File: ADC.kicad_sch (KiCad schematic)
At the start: 28 parts, among them U107 ADR4540, U111 ADA4841-1

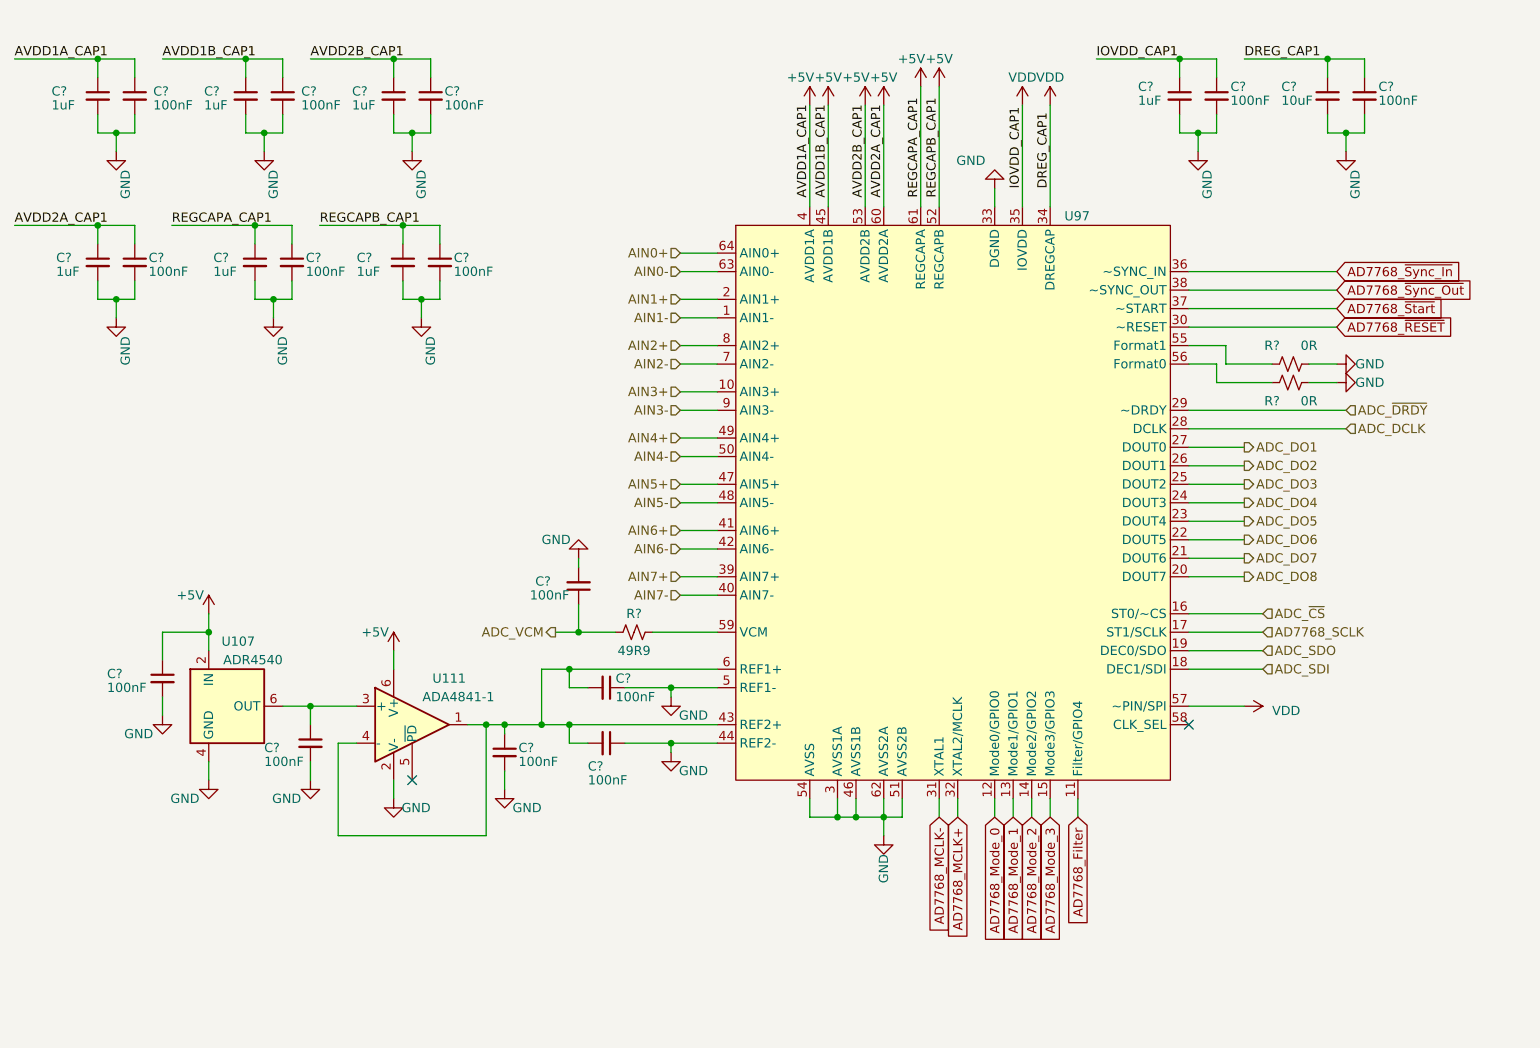
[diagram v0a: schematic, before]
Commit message: Updated Schematics with recent changes
Made Updates with recent suggestions.
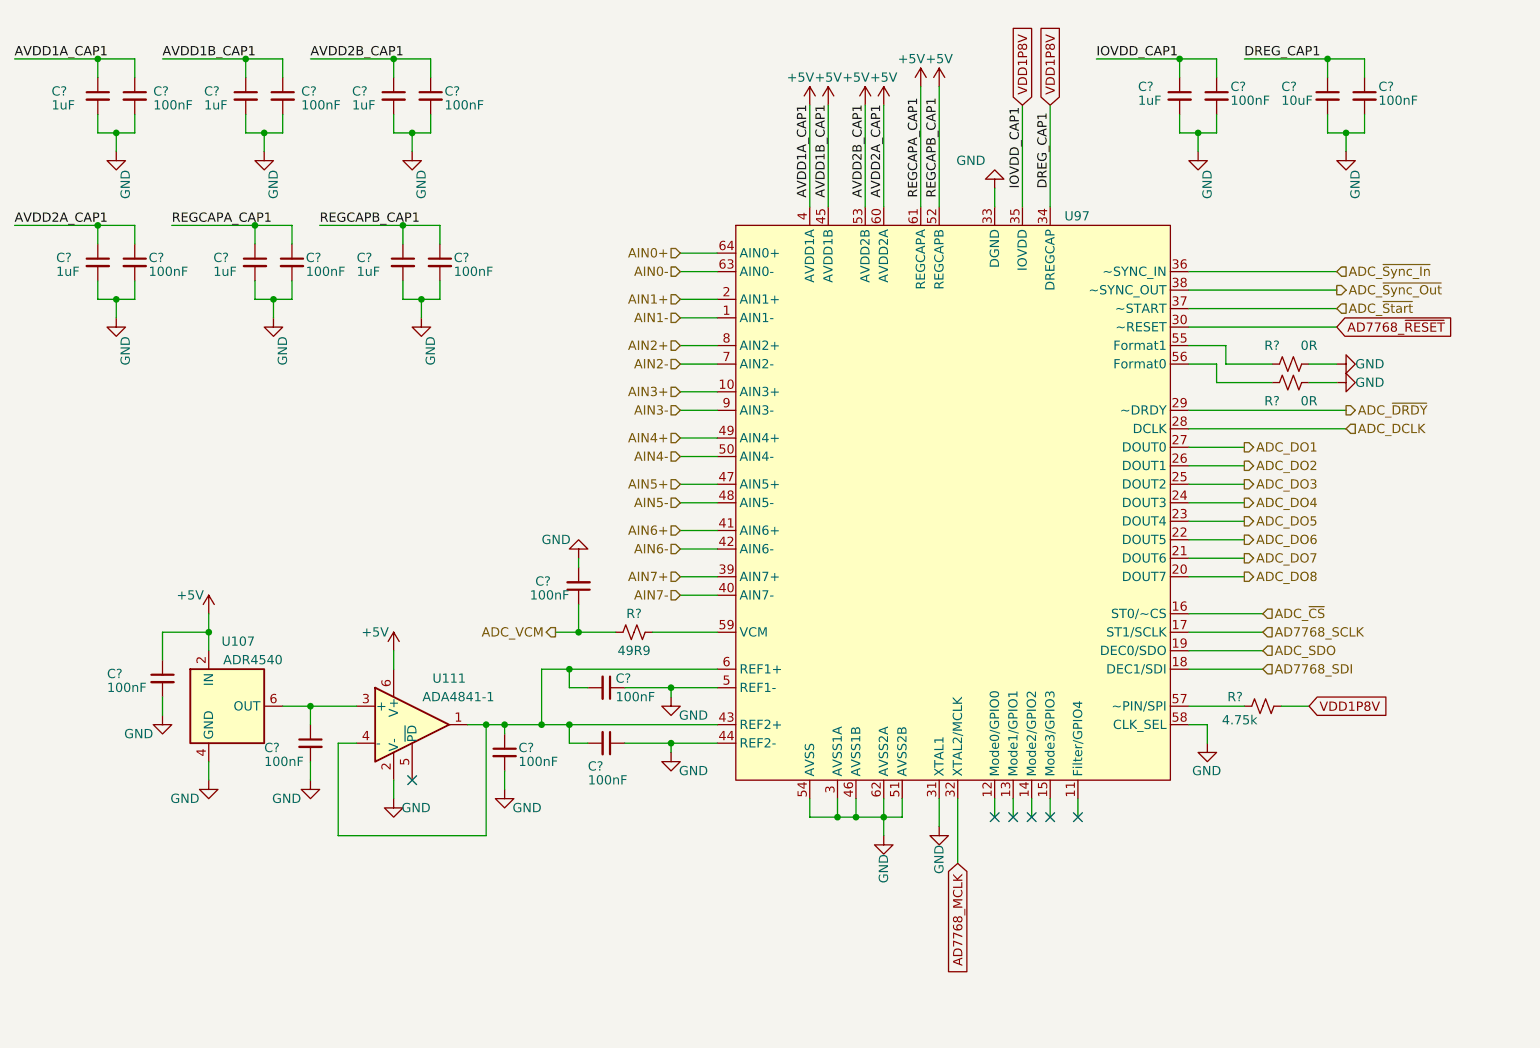
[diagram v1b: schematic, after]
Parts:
- added R?: 4.75k, symbol Device:R_Small_US
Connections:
- net AD7768_MCLK- is gone; now on net GND: U97.31 (XTAL1)
- net GND: now also U97.58 (CLK_SEL)
- net AD7768_Filter: no longer names the net of U97.11 (Filter/GPIO4)
- net AD7768_MCLK+ renamed AD7768_MCLK
- net AD7768_Mode_0: no longer names the net of U97.12 (Mode0/GPIO0)
- net AD7768_Mode_1: no longer names the net of U97.13 (Mode1/GPIO1)
- net AD7768_Mode_2: no longer names the net of U97.14 (Mode2/GPIO2)
- net AD7768_Mode_3: no longer names the net of U97.15 (Mode3/GPIO3)
- net AD7768_~{Start} renamed ADC_~{Start}
- net AD7768_~{Sync_In} renamed ADC_~{Sync_In}
- net AD7768_~{Sync_Out} renamed ADC_~{Sync_Out}
- net ADC_SDI renamed AD7768_SDI
- net VDD renamed VDD1P8V
- net VDD1P8V: now also R?.1; no longer U97.57 (~PIN/SPI)
- new net: R?.2, U97.57 (~PIN/SPI)
- no-connect marks 2 -> 6

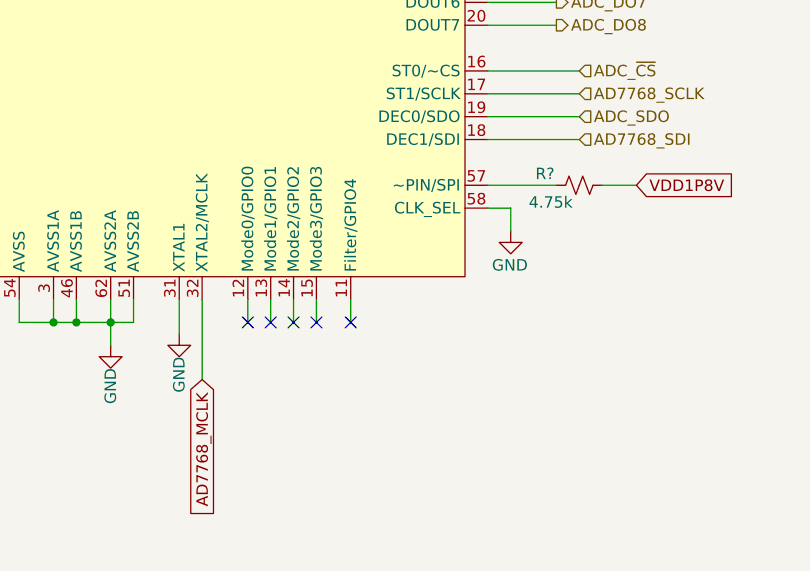
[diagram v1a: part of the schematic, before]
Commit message: Updated Channel 1 and fixes from review
Updated Channel 1 to use the INA851.
Fixed the ORNTA part pinout.
Fixed feedback on LT1763s.
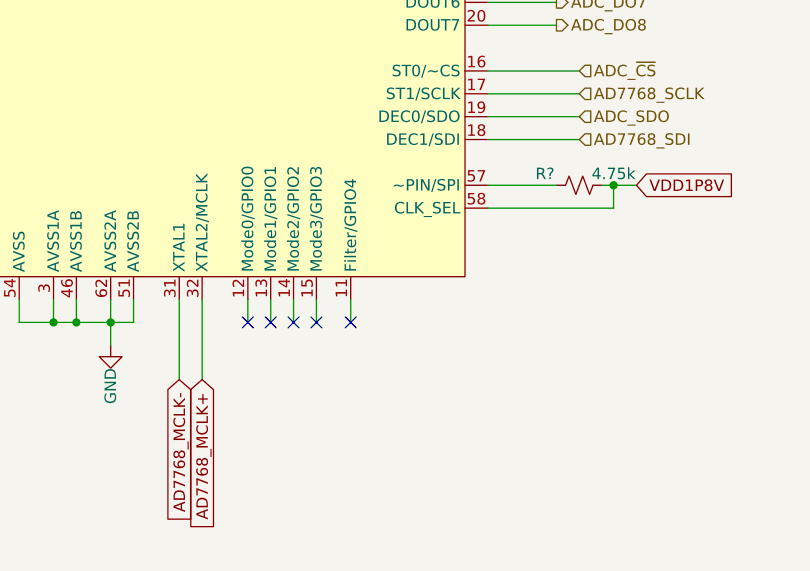
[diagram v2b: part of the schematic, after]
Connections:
- net GND: no longer U97.31 (XTAL1), U97.58 (CLK_SEL)
- net VDD1P8V: now also U97.58 (CLK_SEL)
- net AD7768_MCLK renamed AD7768_MCLK+
- new net AD7768_MCLK-: U97.31 (XTAL1)
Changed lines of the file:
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@@
   (junction (at 170.18 137.16) (diameter 0) (color 0 0 0 0)
+  )
+  (junction (at 226.06 121.92) (diameter 0) (color 0 0 0 0)
   )
   (junction (at 83.82 55.88) (diameter 0) (color 0 0 0 0)
@@
     (stroke (width 0) (type default))
   )
+  (wire (pts (xy 226.06 121.92) (xy 228.6 121.92))
+    (stroke (width 0) (type default))
+  )
   (wire (pts (xy 212.09 101.6) (xy 219.71 101.6))
     (stroke (width 0) (type default))
@@
     (stroke (width 0) (type default))
   )
-  (wire (pts (xy 214.63 127) (xy 214.63 124.46))
-    (stroke (width 0) (type default))
-  )
   (wire (pts (xy 142.24 106.68) (xy 147.32 106.68))
     (stroke (width 0) (type default))
@@
     (stroke (width 0) (type default))
   )
+  (wire (pts (xy 226.06 124.46) (xy 226.06 121.92))
+    (stroke (width 0) (type default))
+  )
   (wire (pts (xy 127 124.46) (xy 147.32 124.46))
     (stroke (width 0) (type default))
@@
     (stroke (width 0) (type default))
   )
-  (wire (pts (xy 224.79 121.92) (xy 228.6 121.92))
+  (wire (pts (xy 224.79 121.92) (xy 226.06 121.92))
     (stroke (width 0) (type default))
   )
@@
     (stroke (width 0) (type default))
   )
-  (wire (pts (xy 177.8 134.62) (xy 177.8 138.43))
+  (wire (pts (xy 177.8 134.62) (xy 177.8 143.51))
     (stroke (width 0) (type default))
   )
@@
     (stroke (width 0) (type default))
   )
-  (wire (pts (xy 214.63 124.46) (xy 212.09 124.46))
+  (wire (pts (xy 212.09 124.46) (xy 226.06 124.46))
     (stroke (width 0) (type default))
   )
@@
     (effects (font (size 1.27 1.27)) (justify left bottom))
   )
-  (global_label "AD7768_MCLK" (shape input) (at 180.34 143.51 270) (fields_autoplaced)
+  (global_label "AD7768_MCLK+" (shape input) (at 180.34 143.51 270) (fields_autoplaced)
     (effects (font (size 1.27 1.27)) (justify right))
-    (property "Intersheetrefs" "${INTERSHEET_REFS}" (at 180.34 159.6789 90)
+    (property "Intersheetrefs" "${INTERSHEET_REFS}" (at 180.34 161.2513 90)
       (effects (font (size 1.27 1.27)) (justify right) hide)
     )
@@
     )
   )
+  (global_label "AD7768_MCLK-" (shape input) (at 177.8 143.51 270) (fields_autoplaced)
+    (effects (font (size 1.27 1.27)) (justify right))
+    (property "Intersheetrefs" "${INTERSHEET_REFS}" (at 177.8 161.2513 90)
+      (effects (font (size 1.27 1.27)) (justify right) hide)
+    )
+  )
   (global_label "VDD1P8V" (shape input) (at 228.6 121.92 0) (fields_autoplaced)
     (effects (font (size 1.27 1.27)) (justify left))
@@
   (hierarchical_label "AIN7-" (shape input) (at 142.24 106.68 180) (fields_autoplaced)
     (effects (font (size 1.27 1.27)) (justify right))
-  )
-  (symbol (lib_id "power:GND") (at 177.8 138.43 0) (unit 1)
-    (in_bom yes) (on_board yes) (dnp no)
-    (property "Reference" "#PWR?" (at 177.8 144.78 0)
-      (effects (font (size 1.27 1.27)) hide)
-    )
-    (property "Value" "GND" (at 177.8 140.97 90)
-      (effects (font (size 1.27 1.27)) (justify right))
-    )
-    (property "Footprint" "" (at 177.8 138.43 0)
-      (effects (font (size 1.27 1.27)) hide)
-    )
-    (property "Datasheet" "" (at 177.8 138.43 0)
-      (effects (font (size 1.27 1.27)) hide)
-    )
-    (pin "1")
-    (instances
-      (project "AD7768_Digitizer"
-        (path "/22331033-57f4-4030-9571-3120e4a10c04"
-          (reference "#PWR?") (unit 1)
-        )
-        (path "/22331033-57f4-4030-9571-3120e4a10c04/852bdf52-52ff-472d-a64d-74fe00f82685"
-          (reference "#PWR?") (unit 1)
-        )
-        (path "/22331033-57f4-4030-9571-3120e4a10c04/68b2b013-abce-4bda-8939-c76bf5b569c5"
-          (reference "#PWR074") (unit 1)
-        )
-        (path "/22331033-57f4-4030-9571-3120e4a10c04/1559db2b-8c6a-417a-873f-12966016a9d4"
-          (reference "#PWR0435") (unit 1)
-        )
-      )
-      (project "Quartz_v1p1"
-        (path "/674e1e7f-67ba-4e85-a926-dcd5f6a22021/c1293333-1878-4cba-a3bd-0c7884de1f1a"
-          (reference "#PWR0238") (unit 1)
-        )
-        (path "/674e1e7f-67ba-4e85-a926-dcd5f6a22021/0ad4247f-0bc9-46d8-8592-1ad068754e52"
-          (reference "#PWR0239") (unit 1)
-        )
-        (path "/674e1e7f-67ba-4e85-a926-dcd5f6a22021/034c4ec3-7306-4a2d-9f0e-d4698fafacde"
-          (reference "#PWR0240") (unit 1)
-        )
-        (path "/674e1e7f-67ba-4e85-a926-dcd5f6a22021/bfc16abb-8eb5-4f14-85a3-701b0b16e6f9"
-          (reference "#PWR0241") (unit 1)
-        )
-      )
-    )
   )
   (symbol (lib_id "power:+5V") (at 175.26 36.83 0) (unit 1)
@@
     )
   )
-  (symbol (lib_id "power:GND") (at 214.63 127 0) (unit 1)
-    (in_bom yes) (on_board yes) (dnp no)
-    (property "Reference" "#PWR?" (at 214.63 133.35 0)
-      (effects (font (size 1.27 1.27)) hide)
-    )
-    (property "Value" "GND" (at 216.535 130.81 0)
-      (effects (font (size 1.27 1.27)) (justify right))
-    )
-    (property "Footprint" "" (at 214.63 127 0)
-      (effects (font (size 1.27 1.27)) hide)
-    )
-    (property "Datasheet" "" (at 214.63 127 0)
-      (effects (font (size 1.27 1.27)) hide)
-    )
-    (pin "1")
-    (instances
-      (project "AD7768_Digitizer"
-        (path "/22331033-57f4-4030-9571-3120e4a10c04"
-          (reference "#PWR?") (unit 1)
-        )
-        (path "/22331033-57f4-4030-9571-3120e4a10c04/852bdf52-52ff-472d-a64d-74fe00f82685"
-          (reference "#PWR?") (unit 1)
-        )
-        (path "/22331033-57f4-4030-9571-3120e4a10c04/68b2b013-abce-4bda-8939-c76bf5b569c5"
-          (reference "#PWR074") (unit 1)
-        )
-        (path "/22331033-57f4-4030-9571-3120e4a10c04/1559db2b-8c6a-417a-873f-12966016a9d4"
-          (reference "#PWR0435") (unit 1)
-        )
-      )
-      (project "Quartz_v1p1"
-        (path "/674e1e7f-67ba-4e85-a926-dcd5f6a22021/c1293333-1878-4cba-a3bd-0c7884de1f1a"
-          (reference "#PWR0242") (unit 1)
-        )
-        (path "/674e1e7f-67ba-4e85-a926-dcd5f6a22021/0ad4247f-0bc9-46d8-8592-1ad068754e52"
-          (reference "#PWR0243") (unit 1)
-        )
-        (path "/674e1e7f-67ba-4e85-a926-dcd5f6a22021/034c4ec3-7306-4a2d-9f0e-d4698fafacde"
-          (reference "#PWR0244") (unit 1)
-        )
-        (path "/674e1e7f-67ba-4e85-a926-dcd5f6a22021/bfc16abb-8eb5-4f14-85a3-701b0b16e6f9"
-          (reference "#PWR0245") (unit 1)
-        )
-      )
-    )
-  )
   (symbol (lib_id "power:+5V") (at 177.8 36.83 0) (unit 1)
     (in_bom yes) (on_board yes) (dnp no)
@@
       (effects (font (size 1.27 1.27)))
     )
-    (property "Value" "4.75k" (at 219.075 123.825 90)
+    (property "Value" "4.75k" (at 226.06 120.65 90)
       (effects (font (size 1.27 1.27)))
     )

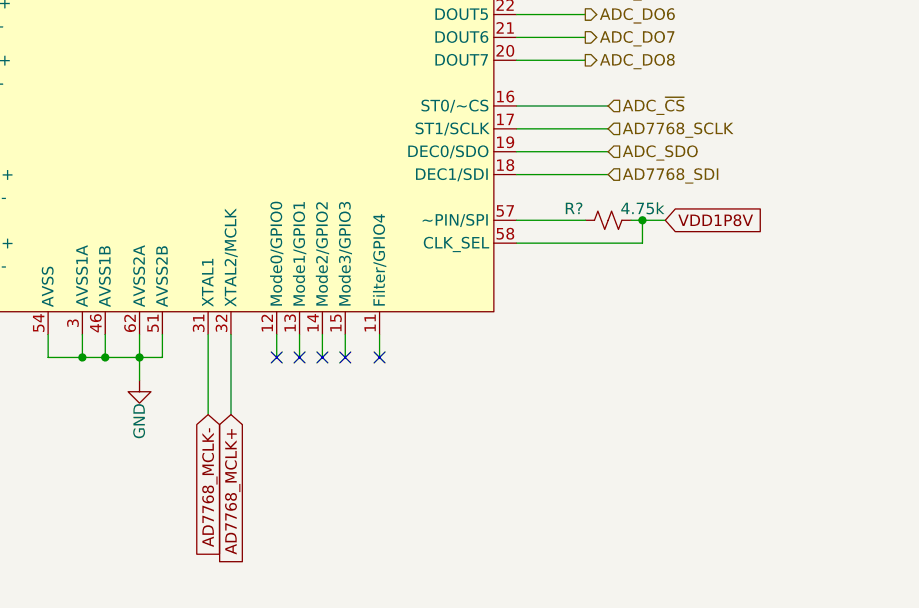
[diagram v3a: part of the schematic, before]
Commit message: Updated Schematics
Changes:
-Moved Input resistors to after Coupling Relay
-Added diff cap at ADC input
-Changed the ADC clocking configuration (added quad LVDS driver)
-Changed some signal names for consistancy
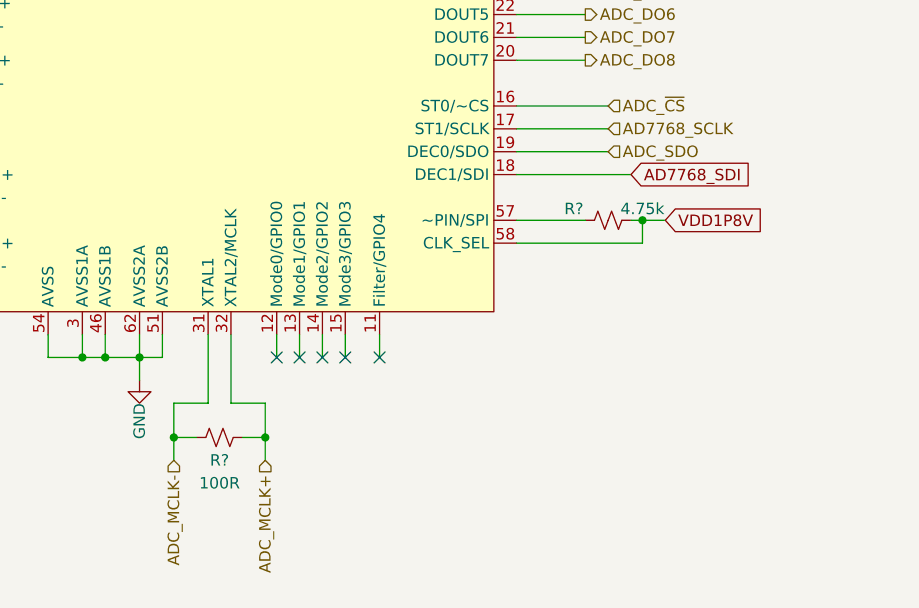
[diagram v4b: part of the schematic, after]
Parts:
- added R?: 100R, symbol Device:R_Small_US
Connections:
- net AD7768_MCLK+ renamed ADC_MCLK+
- net ADC_MCLK+: now also R?.1
- net AD7768_MCLK- renamed ADC_MCLK-
- net ADC_MCLK-: now also R?.2

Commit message: Updated Schematics with latest suggestions
updates:
-Revised Power supply section
-Changed clock buffer chip for ADC Clock
- Added additional no pop & jumper parts for board debugging
-Other small part changes
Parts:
- removed R?: 100R, symbol Device:R_Small_US
- added C?: 100nF, Capacitor_SMD:C_0603_1608Metric, symbol Device:C_Small
- added R? (x2): open, Resistor_SMD:R_0603_1608Metric, symbol Device:R_Small_US
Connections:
- net +5V: now also C?.1
- net ADC_MCLK+: now also R?.2
- net ADC_MCLK-: now also R?.1
- net GND: now also C?.2, R?.2
- net at U97.11 (Filter/GPIO4): now also R?.1
- no-connect marks 6 -> 5

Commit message: Schematic Updates
Updated:
-Fixed AMC7823 labels
-Added present detect signals on FMC
-Added ferrite beads in Power Section and AFE
-Added 0R in power section
-Revised EEPROM connections
-Changed +5V SMPS part to one with an integrated inductor
-Added more detail on FMC connector
-Added file showing SMPS calculations
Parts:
- U97: value ~ -> AD7768; MPN (none) -> AD7768BSTZ

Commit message: Updated Schematic
-Changed PPS input signal buffer
-Made Tweaks to Power Supply section  (Many involving the LT3097) as suggested by Trent.
- general schematic clean up for readability
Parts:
- R? (x2): MPN RMCF0603ZT0R00 -> ERJ-3GEY0R00V
- R?: MPN (none) -> RC0603FR-074K75L
- R?: footprint Capacitor_SMD:C_0603_1608Metric -> Resistor_SMD:R_0603_1608Metric
